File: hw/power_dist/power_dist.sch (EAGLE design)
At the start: 69 parts, among them J1 JST-ZH6SMT_VERT, J2 JST-PH4SMT_VERT, J3 JST-PH5VERT, P1 XT30P, P2 XT30P, P3 XT30P, P4 XT30P, P5 XT30P, P6 XT30P, P7 XT90PW-M, Q1 PSMN4R8-100BSEJ, Q2 PSMN4R8-100BSEJ, Q3 PSMN4R8-100BSEJ, Q4 MF-DSC-SOT233-BSS138, Q5 MF-DSC-SOT233-MMBT3906, Q6 MF-DSC-SOT233-MMBT3904, U1 MAX15062AATA+T, U2 STM32G474CEU6, U3 LM5066IPMHE/NOPB, U4 TCAN334G

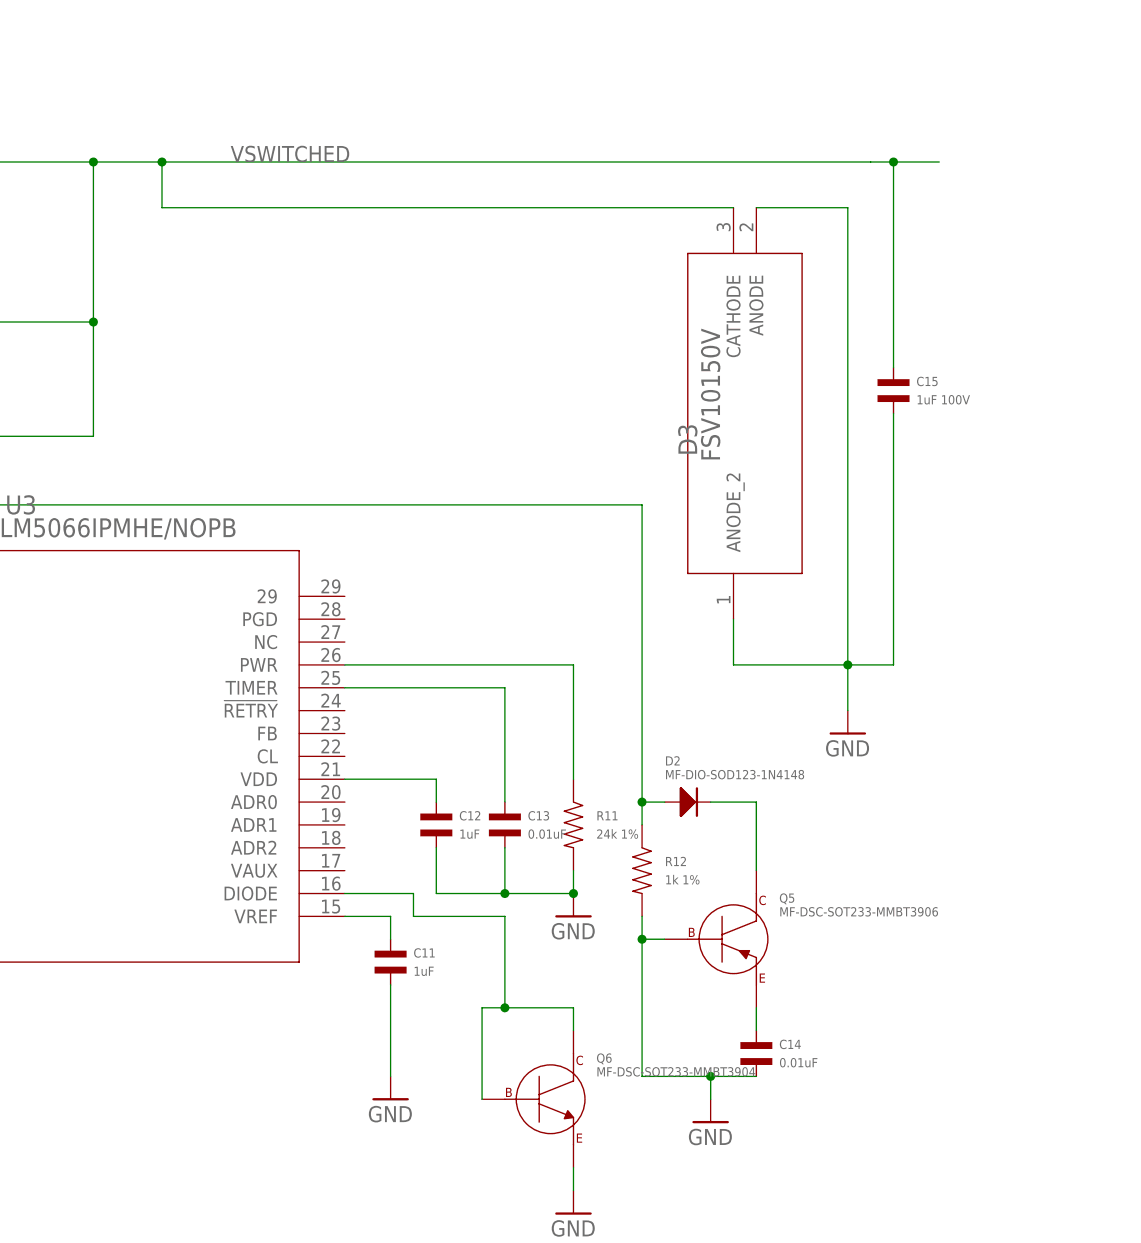
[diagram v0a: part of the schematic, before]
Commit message: power_dist r4: Add some DNP resistors for PGD and FB
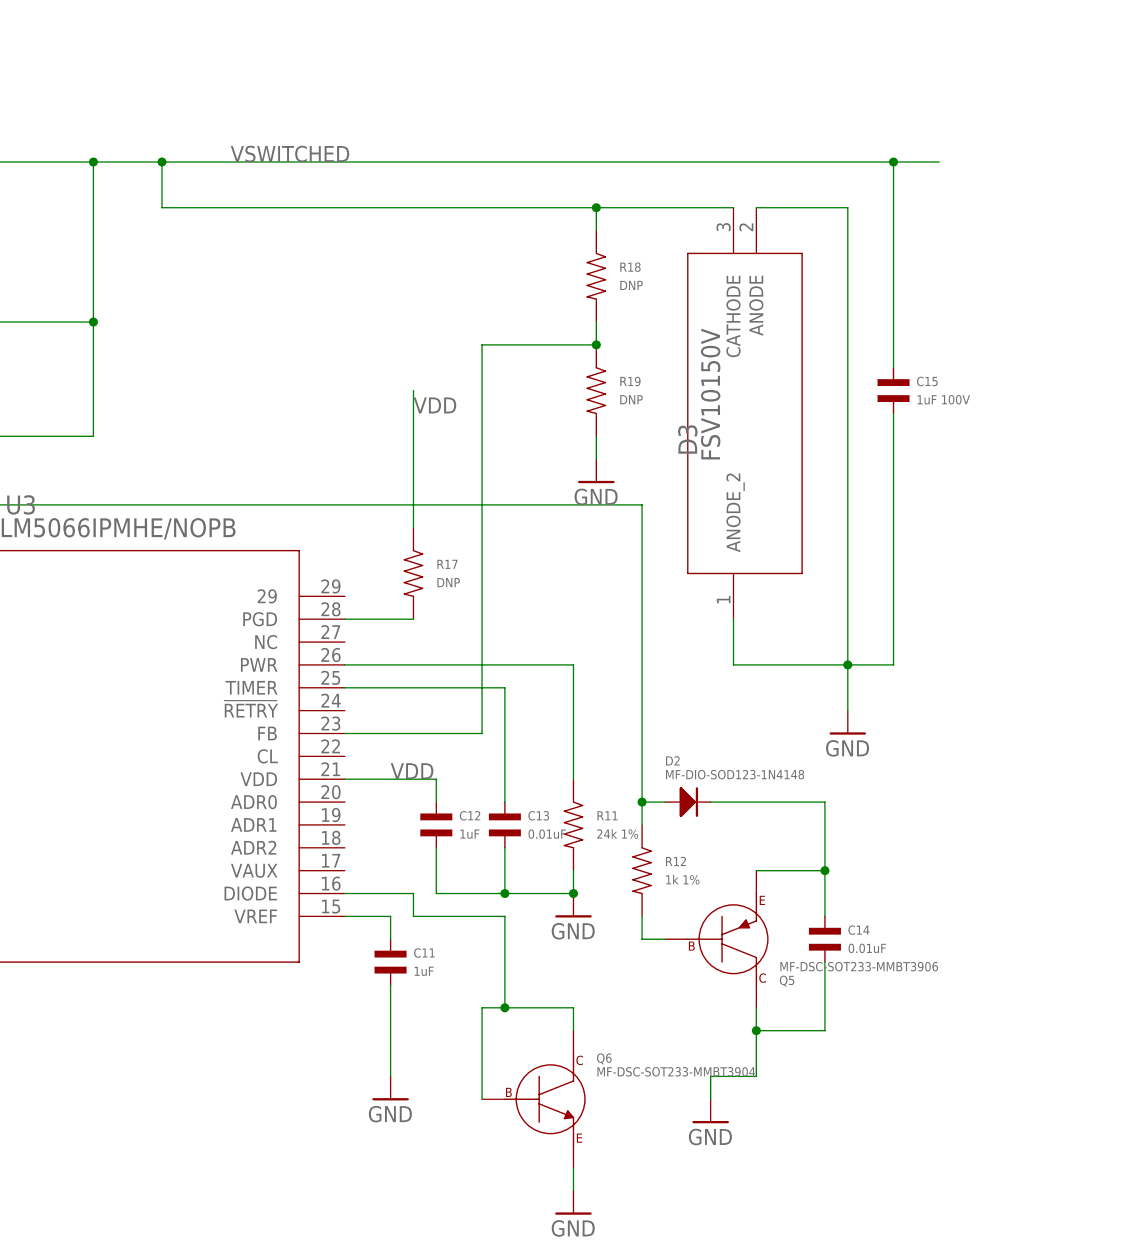
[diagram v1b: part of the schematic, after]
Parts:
- added R17, R18, R19: DNP, mfpassives:RESISTOR_0603
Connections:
- new net N$16: Q5.BASE, R12.P$2
- new net VDD: C12.P$1, R17.P$1, U3.VDD
- net GND: now also Q5.COLLECTOR, R19.P$2; no longer Q5.BASE, R12.P$2
- net N$12: now also R17.P$2, U3.PGD; no longer C14.P$1, Q5.EMITTER
- net N$13: now also C14.P$1, Q5.EMITTER; no longer Q5.COLLECTOR
- net N$6: now also R18.P$2, R19.P$1, U3.FB; no longer C12.P$1, U3.VDD
- net VSWITCHED: now also R18.P$1
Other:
- moved on the sheet: C14, Q5
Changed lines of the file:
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@@
 <attribute name="POPULATE" value="0"/>
 </part>
+<part name="R17" library="mfpassives" deviceset="RESISTOR" device="_0603" value="DNP">
+<attribute name="MF" value=""/>
+<attribute name="POPULATE" value="0"/>
+</part>
+<part name="R18" library="mfpassives" deviceset="RESISTOR" device="_0603" value="DNP">
+<attribute name="MF" value=""/>
+<attribute name="POPULATE" value="0"/>
+</part>
+<part name="R19" library="mfpassives" deviceset="RESISTOR" device="_0603" value="DNP">
+<attribute name="MF" value=""/>
+<attribute name="POPULATE" value="0"/>
+</part>
+<part name="GND27" library="supply1" deviceset="GND" device=""/>
 </parts>
 <sheets>
@@
 <attribute name="VALUE" x="60.96" y="-47.244" size="1.016" layer="96" font="vector"/>
 </instance>
-<instance part="C14" gate="G$1" x="86.36" y="-71.12" smashed="yes">
-<attribute name="NAME" x="88.9" y="-69.596" size="1.016" layer="95" font="vector" align="top-left"/>
-<attribute name="VALUE" x="88.9" y="-72.644" size="1.016" layer="96" font="vector"/>
+<instance part="C14" gate="G$1" x="93.98" y="-58.42" smashed="yes">
+<attribute name="NAME" x="96.52" y="-56.896" size="1.016" layer="95" font="vector" align="top-left"/>
+<attribute name="VALUE" x="96.52" y="-59.944" size="1.016" layer="96" font="vector"/>
 </instance>
 <instance part="R12" gate="G$1" x="73.66" y="-50.8" smashed="yes">
@@
 <attribute name="VALUE" x="76.2" y="-40.64" size="1.016" layer="96" font="vector"/>
 </instance>
-<instance part="Q5" gate="G$1" x="83.82" y="-58.42" smashed="yes">
-<attribute name="NAME" x="88.9" y="-53.34" size="1.016" layer="95" font="vector" rot="R180" align="bottom-right"/>
-<attribute name="VALUE" x="88.9" y="-55.88" size="1.016" layer="96" font="vector"/>
+<instance part="Q5" gate="G$1" x="83.82" y="-58.42" smashed="yes" rot="MR180">
+<attribute name="NAME" x="88.9" y="-63.5" size="1.016" layer="95" font="vector" rot="MR0" align="bottom-right"/>
+<attribute name="VALUE" x="88.9" y="-60.96" size="1.016" layer="96" font="vector" rot="MR180"/>
 </instance>
 <instance part="Q4" gate="G$1" x="-68.58" y="-43.18" smashed="yes">
@@
 <attribute name="NAME" x="10.16" y="164.084" size="1.016" layer="95" font="vector" align="top-left"/>
 <attribute name="VALUE" x="10.16" y="161.036" size="1.016" layer="96" font="vector"/>
+</instance>
+<instance part="R17" gate="G$1" x="48.26" y="-17.78" smashed="yes">
+<attribute name="NAME" x="50.8" y="-16.256" size="1.016" layer="95" font="vector" align="top-left"/>
+<attribute name="VALUE" x="50.8" y="-19.304" size="1.016" layer="96" font="vector"/>
+<attribute name="MF" x="48.26" y="-17.78" size="1.778" layer="96" display="off"/>
+</instance>
+<instance part="R18" gate="G$1" x="68.58" y="15.24" smashed="yes">
+<attribute name="NAME" x="71.12" y="16.764" size="1.016" layer="95" font="vector" align="top-left"/>
+<attribute name="VALUE" x="71.12" y="13.716" size="1.016" layer="96" font="vector"/>
+<attribute name="MF" x="68.58" y="15.24" size="1.778" layer="96" display="off"/>
+</instance>
+<instance part="R19" gate="G$1" x="68.58" y="2.54" smashed="yes">
+<attribute name="NAME" x="71.12" y="4.064" size="1.016" layer="95" font="vector" align="top-left"/>
+<attribute name="VALUE" x="71.12" y="1.016" size="1.016" layer="96" font="vector"/>
+<attribute name="MF" x="68.58" y="2.54" size="1.778" layer="96" display="off"/>
+</instance>
+<instance part="GND27" gate="1" x="68.58" y="-7.62" smashed="yes">
+<attribute name="VALUE" x="66.04" y="-10.16" size="1.778" layer="96"/>
 </instance>
 </instances>
@@
 </segment>
 <segment>
-<pinref part="R12" gate="G$1" pin="P$2"/>
-<wire x1="73.66" y1="-55.88" x2="73.66" y2="-58.42" width="0.1524" layer="91"/>
-<wire x1="73.66" y1="-58.42" x2="73.66" y2="-73.66" width="0.1524" layer="91"/>
-<wire x1="73.66" y1="-73.66" x2="81.28" y2="-73.66" width="0.1524" layer="91"/>
-<pinref part="C14" gate="G$1" pin="P$2"/>
-<wire x1="81.28" y1="-73.66" x2="86.36" y2="-73.66" width="0.1524" layer="91"/>
 <pinref part="GND13" gate="1" pin="GND"/>
 <wire x1="81.28" y1="-73.66" x2="81.28" y2="-76.2" width="0.1524" layer="91"/>
-<junction x="81.28" y="-73.66"/>
-<pinref part="Q5" gate="G$1" pin="BASE"/>
-<wire x1="76.2" y1="-58.42" x2="73.66" y2="-58.42" width="0.1524" layer="91"/>
-<junction x="73.66" y="-58.42"/>
+<pinref part="Q5" gate="G$1" pin="COLLECTOR"/>
+<wire x1="86.36" y1="-66.04" x2="86.36" y2="-68.58" width="0.1524" layer="91"/>
+<wire x1="86.36" y1="-68.58" x2="86.36" y2="-73.66" width="0.1524" layer="91"/>
+<wire x1="86.36" y1="-73.66" x2="81.28" y2="-73.66" width="0.1524" layer="91"/>
+<pinref part="C14" gate="G$1" pin="P$2"/>
+<wire x1="93.98" y1="-60.96" x2="93.98" y2="-68.58" width="0.1524" layer="91"/>
+<wire x1="93.98" y1="-68.58" x2="86.36" y2="-68.58" width="0.1524" layer="91"/>
+<junction x="86.36" y="-68.58"/>
 </segment>
 <segment>
@@
 <wire x1="7.62" y1="154.94" x2="0" y2="154.94" width="0.1524" layer="91"/>
 <junction x="0" y="154.94"/>
+</segment>
+<segment>
+<pinref part="GND27" gate="1" pin="GND"/>
+<pinref part="R19" gate="G$1" pin="P$2"/>
+<wire x1="68.58" y1="-2.54" x2="68.58" y2="-5.08" width="0.1524" layer="91"/>
 </segment>
 </net>
@@
 <pinref part="D3" gate="A" pin="CATHODE"/>
 <wire x1="12.7" y1="10.16" x2="12.7" y2="27.94" width="0.1524" layer="91"/>
-<wire x1="83.82" y1="22.86" x2="20.32" y2="22.86" width="0.1524" layer="91"/>
+<wire x1="83.82" y1="22.86" x2="68.58" y2="22.86" width="0.1524" layer="91"/>
+<wire x1="68.58" y1="22.86" x2="20.32" y2="22.86" width="0.1524" layer="91"/>
 <wire x1="20.32" y1="22.86" x2="20.32" y2="27.94" width="0.1524" layer="91"/>
 <junction x="20.32" y="27.94"/>
@@
 <wire x1="-2.54" y1="-2.54" x2="12.7" y2="-2.54" width="0.1524" layer="91"/>
 <wire x1="12.7" y1="-2.54" x2="12.7" y2="10.16" width="0.1524" layer="91"/>
-<wire x1="20.32" y1="27.94" x2="99.06" y2="27.94" width="0.1524" layer="91"/>
+<wire x1="20.32" y1="27.94" x2="101.6" y2="27.94" width="0.1524" layer="91"/>
 <wire x1="101.6" y1="27.94" x2="106.68" y2="27.94" width="0.1524" layer="91"/>
 <wire x1="-2.54" y1="-2.54" x2="-2.54" y2="-12.7" width="0.1524" layer="91"/>
@@
 <pinref part="C15" gate="G$1" pin="P$1"/>
 <wire x1="101.6" y1="5.08" x2="101.6" y2="27.94" width="0.1524" layer="91"/>
-<wire x1="101.6" y1="27.94" x2="99.06" y2="27.94" width="0.1524" layer="91"/>
 <junction x="101.6" y="27.94"/>
 <junction x="-2.54" y="-2.54"/>
+<pinref part="R18" gate="G$1" pin="P$1"/>
+<wire x1="68.58" y1="20.32" x2="68.58" y2="22.86" width="0.1524" layer="91"/>
+<junction x="68.58" y="22.86"/>
 </segment>
 <segment>
@@
 </segment>
 </net>
-<net name="N$12" class="0">
-<segment>
+<net name="N$13" class="0">
+<segment>
+<pinref part="D2" gate="G$1" pin="CATHODE"/>
+<wire x1="93.98" y1="-43.18" x2="81.28" y2="-43.18" width="0.1524" layer="91"/>
 <pinref part="Q5" gate="G$1" pin="EMITTER"/>
+<wire x1="86.36" y1="-50.8" x2="93.98" y2="-50.8" width="0.1524" layer="91"/>
 <pinref part="C14" gate="G$1" pin="P$1"/>
-<wire x1="86.36" y1="-66.04" x2="86.36" y2="-68.58" width="0.1524" layer="91"/>
-</segment>
-</net>
-<net name="N$13" class="0">
-<segment>
-<pinref part="Q5" gate="G$1" pin="COLLECTOR"/>
-<wire x1="86.36" y1="-50.8" x2="86.36" y2="-43.18" width="0.1524" layer="91"/>
-<pinref part="D2" gate="G$1" pin="CATHODE"/>
-<wire x1="86.36" y1="-43.18" x2="81.28" y2="-43.18" width="0.1524" layer="91"/>
+<wire x1="93.98" y1="-50.8" x2="93.98" y2="-55.88" width="0.1524" layer="91"/>
+<wire x1="93.98" y1="-43.18" x2="93.98" y2="-50.8" width="0.1524" layer="91"/>
+<junction x="93.98" y="-50.8"/>
 </segment>
 </net>
@@
 </segment>
 </net>
-<net name="N$6" class="0">
+<net name="VDD" class="0">
 <segment>
 <pinref part="U3" gate="A" pin="VDD"/>
@@
 <wire x1="50.8" y1="-40.64" x2="50.8" y2="-43.18" width="0.1524" layer="91"/>
 <pinref part="C12" gate="G$1" pin="P$1"/>
+<label x="45.72" y="-40.64" size="1.778" layer="95"/>
+</segment>
+<segment>
+<pinref part="R17" gate="G$1" pin="P$1"/>
+<wire x1="48.26" y1="-12.7" x2="48.26" y2="2.54" width="0.1524" layer="91"/>
+<label x="48.26" y="0" size="1.778" layer="95"/>
 </segment>
 </net>
@@
 </segment>
 </net>
+<net name="N$16" class="0">
+<segment>
+<pinref part="R12" gate="G$1" pin="P$2"/>
+<wire x1="73.66" y1="-55.88" x2="73.66" y2="-58.42" width="0.1524" layer="91"/>
+<pinref part="Q5" gate="G$1" pin="BASE"/>
+<wire x1="76.2" y1="-58.42" x2="73.66" y2="-58.42" width="0.1524" layer="91"/>
+</segment>
+</net>
+<net name="N$12" class="0">
+<segment>
+<pinref part="U3" gate="A" pin="PGD"/>
+<pinref part="R17" gate="G$1" pin="P$2"/>
+<wire x1="40.64" y1="-22.86" x2="48.26" y2="-22.86" width="0.1524" layer="91"/>
+</segment>
+</net>
+<net name="N$6" class="0">
+<segment>
+<pinref part="R19" gate="G$1" pin="P$1"/>
+<pinref part="R18" gate="G$1" pin="P$2"/>
+<wire x1="68.58" y1="10.16" x2="68.58" y2="7.62" width="0.1524" layer="91"/>
+<pinref part="U3" gate="A" pin="FB"/>
+<wire x1="40.64" y1="-35.56" x2="55.88" y2="-35.56" width="0.1524" layer="91"/>
+<wire x1="55.88" y1="-35.56" x2="55.88" y2="7.62" width="0.1524" layer="91"/>
+<wire x1="55.88" y1="7.62" x2="68.58" y2="7.62" width="0.1524" layer="91"/>
+<junction x="68.58" y="7.62"/>
+</segment>
+</net>
